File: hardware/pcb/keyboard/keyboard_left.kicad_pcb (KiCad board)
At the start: 2 copper layers, 133.8 x 110.4 mm, 109 parts, among them J1 SM04B-SRSS-TB, J2 PJ320D, J3 HRO_TYPE-C-31-M-12, J4 FH34SRJ-10S-0.5SH, SW29 PTS845, U1 74HC4051, U2 OPA350UA, U3 DT1446-04S, U4 XC6220B331MR-G, U5 STM32G0B1KETx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

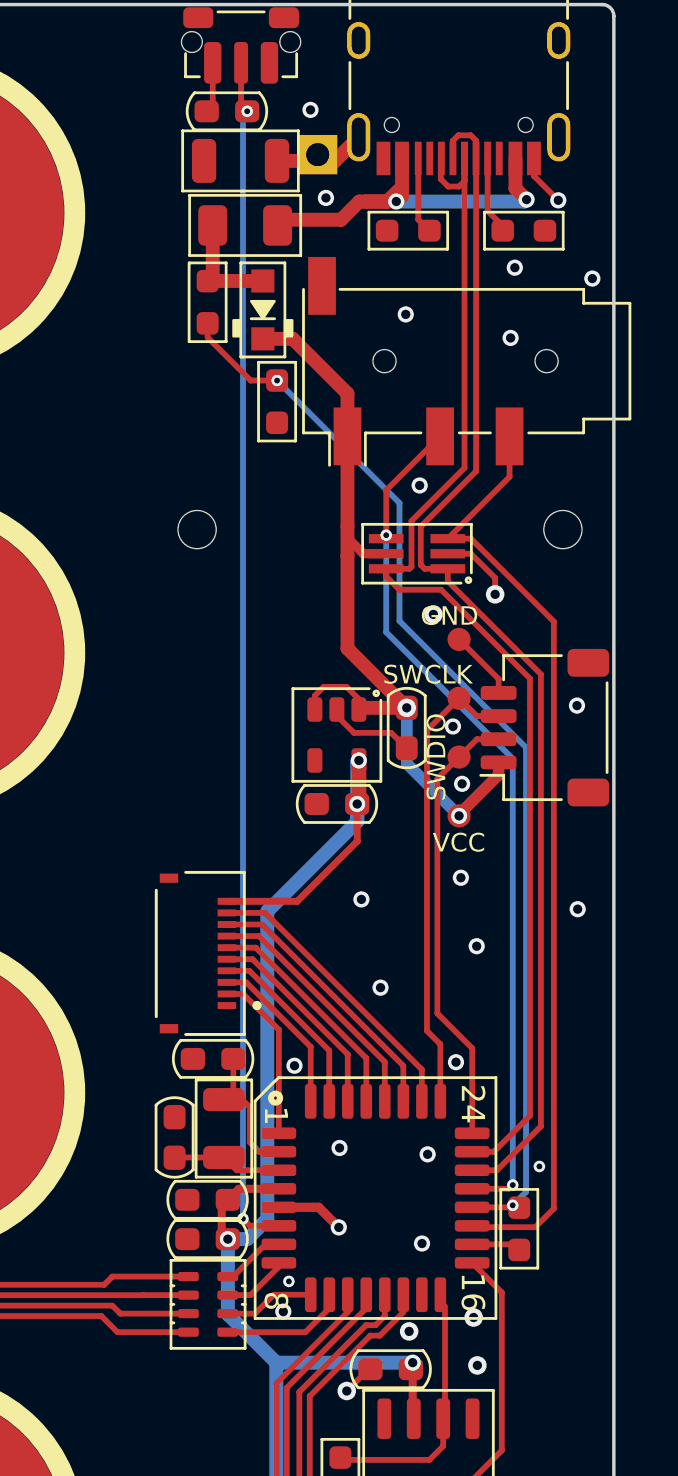
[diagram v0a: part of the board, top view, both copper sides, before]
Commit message: roate FFC Connector
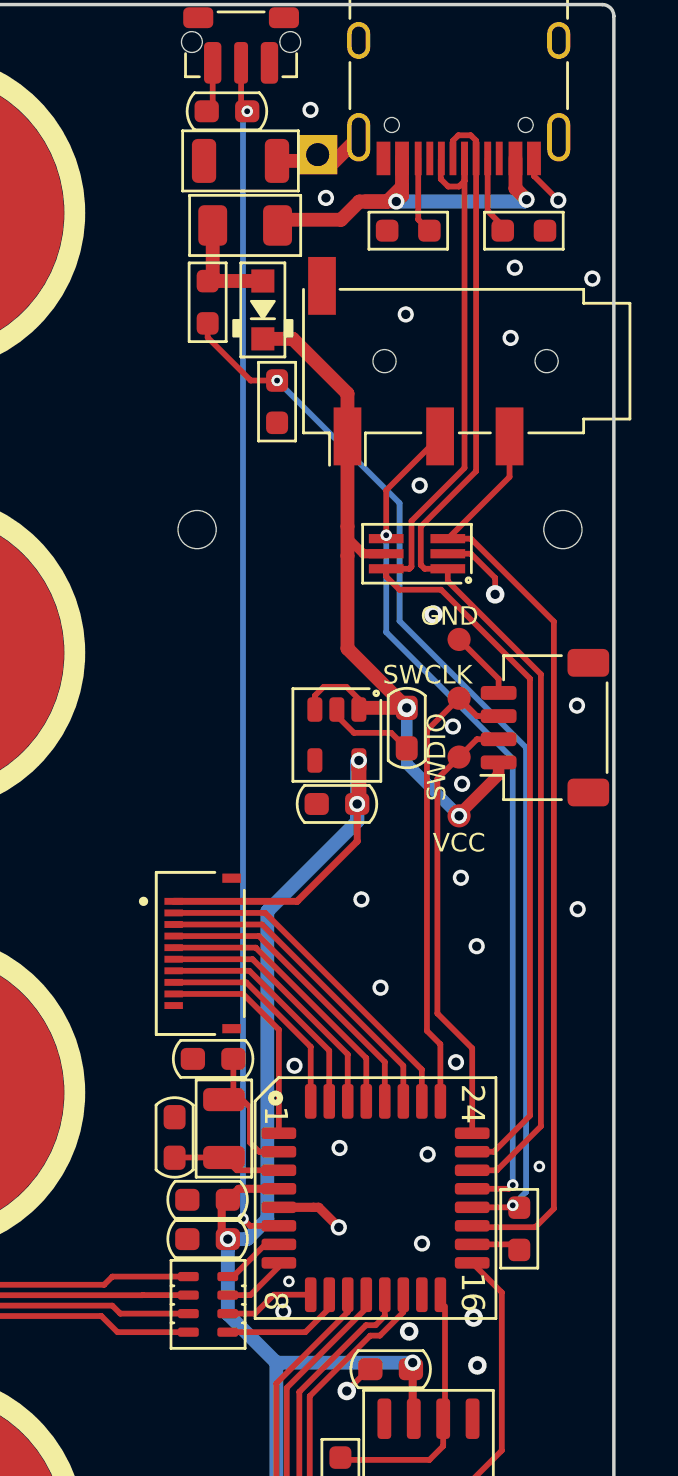
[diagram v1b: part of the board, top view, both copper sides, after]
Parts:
- turned J4 to 90 degrees
- turned RN3 to 180 degrees
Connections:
- net Handness renamed Handedness
- J4 pad 1: GND -> +3V3
- J4 pad 10: +3V3 -> GND
- J4 pad 2: ACCS_8 -> ACCS_1
- J4 pad 3: ACCS_7 -> ACCS_2
- J4 pad 4: ACCS_6 -> ACCS_3
- J4 pad 5: ACCS_5 -> ACCS_4
- J4 pad 6: ACCS_4 -> ACCS_5
- J4 pad 7: ACCS_3 -> ACCS_6
- J4 pad 8: ACCS_2 -> ACCS_7
- J4 pad 9: ACCS_1 -> ACCS_8
- RN3 pad 1: TX0 -> TX3
- RN3 pad 2: TX1 -> TX2
- RN3 pad 3: TX2 -> TX1
- RN3 pad 4: TX3 -> TX0
- RN3 pad 5: ROW3 -> ROW0
- RN3 pad 6: ROW2 -> ROW1
- RN3 pad 7: ROW1 -> ROW2
- RN3 pad 8: ROW0 -> ROW3
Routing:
- net +3V3: track 74.1 -> 76.5 mm
- net ACCS_8: track 7.35 -> 9.65 mm
- net ACCS_6: track 8.04 -> 10.3 mm
- net ACCS_5: track 8.95 -> 11.3 mm
- net ACCS_4: track 9.86 -> 12.2 mm
- net ACCS_3: track 10.8 -> 13.1 mm
- net ACCS_2: track 11.7 -> 14.0 mm
- net ACCS_1: track 12.6 -> 14.9 mm
- net ACCS_7: track 7.13 -> 9.43 mm

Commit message: temp
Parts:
- removed R1, R5: 1k, PCM_Resistor_SMD_AKL:R_0603_1608Metric_Pad0.98x0.95mm
- removed R4: < 800, PCM_Resistor_SMD_AKL:R_0603_1608Metric_Pad0.98x0.95mm
- added C11: 1uF, PCM_Capacitor_SMD_AKL:C_0603_1608Metric, F.Cu at (187.9, 55.0)
- added C12: 22p, PCM_Capacitor_SMD_AKL:C_0603_1608Metric, F.Cu at (183.5, 52.5)
- added C13: 22p, PCM_Capacitor_SMD_AKL:C_0603_1608Metric, F.Cu at (182.8, 58.2)
- added C14: 1uF, PCM_Capacitor_SMD_AKL:C_0603_1608Metric, F.Cu at (186.4, 55.0)
- added C16: 100n, PCM_Capacitor_SMD_AKL:C_0603_1608Metric, F.Cu at (193.3, 84.8)
- added C17: 1u, PCM_Capacitor_SMD_AKL:C_0603_1608Metric, F.Cu at (193.3, 86.6)
- added FB1: 1k 100mhz, Inductor_SMD:L_0603_1608Metric, F.Cu at (195.6, 85.6)
- added R8: 10k, PCM_Resistor_SMD_AKL:R_0603_1608Metric, F.Cu at (182.1, 80.0)
- added U6: CH334R, Package_SO:QSOP-16_3.9x4.9mm_P0.635mm, F.Cu at (187.4, 60.3)
- added Y2: 8MHz, PCM_Crystal_Handsoldering_AKL:Crystal_SMD_2520-4Pin_2.5x2.0mm, F.Cu at (183.7, 55.0)
- C1, C10, C2, C3, C4, C6, C7, C8, C9: footprint PCM_Capacitor_SMD_AKL:C_0603_1608Metric_Pad1.05x0.95mm -> PCM_Capacitor_SMD_AKL:C_0603_1608Metric
- C5: value 4.7u -> 0.1uF; footprint PCM_Capacitor_SMD_AKL:C_0603_1608Metric_Pad1.05x0.95mm -> PCM_Capacitor_SMD_AKL:C_0603_1608Metric
- R2, R3, R6, R7: footprint PCM_Resistor_SMD_AKL:R_0603_1608Metric_Pad0.98x0.95mm -> PCM_Resistor_SMD_AKL:R_0603_1608Metric
- U5: value STM32G0B1KETx -> STM32G431KBTx; footprint PCM_Package_QFP_AKL:LQFP-32_7x7mm_P0.8mm -> Package_QFP:LQFP-32_7x7mm_P0.8mm
- Y1: value NX3215SA -> 8MHz; footprint PCM_Crystal_AKL:Crystal_SMD_3215-2Pin_3.2x1.5mm -> PCM_Crystal_Handsoldering_AKL:Crystal_SMD_2520-4Pin_2.5x2.0mm
- moved H14 15.8 mm to (182.0, 48.9)
- moved H15 15.8 mm to (197.8, 48.9)
- moved C4 12.8 mm to (195.1, 83.1), turned to 0 degrees
- moved C8 9.40 mm to (186.9, 52.5), turned to 0 degrees
- moved U4 9.29 mm to (186.6, 49.7), turned to 180 degrees
- moved C9 6.87 mm to (189.5, 51.9)
- moved C5 5.88 mm to (185.1, 73.7), turned to 90 degrees
- moved D1 4.60 mm to (185.0, 45.1)
- moved F1 3.69 mm to (185.0, 40.4), turned to 90 degrees
- moved C7 2.46 mm to (182.4, 78.3), turned to 180 degrees
- moved U3 1.83 mm to (192.8, 49.7)
- moved L1 1.71 mm to (185.0, 35.4), turned to 90 degrees
- moved C1 1.47 mm to (184.8, 31.9), turned to 180 degrees
- moved R6 1.44 mm to (186.8, 94.2)
- moved C2 1.38 mm to (189.0, 86.3)
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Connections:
- C6 pad 2: /OSC32_IN -> Net-(U5-PF0)
- C7 pad 2: /OSC32_OUT -> Net-(U5-PF1)
- D1 pad 2: Net-(D1-A) -> VBUS
- F1 pad 1: Net-(D1-A) -> VBUS
- F1 pad 2: VBUS -> Net-(F1-Pad2)
- J1 pad 1: +5V -> +3V3
- J3 pad A4: VBUS -> Net-(F1-Pad2)
- J3 pad A6: D+ -> /UP_D+
- J3 pad A7: D- -> /UP_D-
- J3 pad A9: VBUS -> Net-(F1-Pad2)
- J3 pad B4: VBUS -> Net-(F1-Pad2)
- J3 pad B6: D+ -> /UP_D+
- J3 pad B7: D- -> /UP_D-
- J3 pad B9: VBUS -> Net-(F1-Pad2)
- J4 pad 2: ACCS_1 -> unconnected-(J4-Pin_2-Pad2)
- J4 pad 3: ACCS_2 -> ACCS_1
- J4 pad 4: ACCS_3 -> ACCS_2
- J4 pad 5: ACCS_4 -> ACCS_3
- J4 pad 6: ACCS_5 -> ACCS_4
- J4 pad 7: ACCS_6 -> ACCS_5
- J4 pad 8: ACCS_7 -> ACCS_6
- J4 pad 9: ACCS_8 -> ACCS_7
- TP1 pad 1: +5V -> +3V3
- U3 pad 1: D- -> USART_RX
- U3 pad 4: USART_RX -> /UP_D-
- U3 pad 6: D+ -> /UP_D+
- U5 pad 1: ACCS_8 -> +3V3
- U5 pad 10: TX3 -> CSEL1
- U5 pad 11: CSEL0 -> CSEL2
- U5 pad 12: CSEL1 -> CSEL_EN
- U5 pad 13: CSEL2 -> ADC
- U5 pad 14: CSEL_EN -> GND
- U5 pad 15: /ADC1_IN8 -> VDDA
- U5 pad 16: ADC -> GND
- U5 pad 17: CHARGE_RST -> +3V3
- U5 pad 18: Handedness -> CHARGE_RST
- U5 pad 2: /OSC32_IN -> Net-(U5-PF0)
- U5 pad 20: VBUS_DEC -> USART_RX
- U5 pad 21: USART_RX -> /MCU_D-
- U5 pad 22: D- -> /MCU_D+
- U5 pad 23: D+ -> SWDIO
- U5 pad 24: SWDIO -> SWCLK
- U5 pad 25: SWCLK -> ACCS_1
- U5 pad 26: ACCS_1 -> ACCS_2
- U5 pad 27: ACCS_2 -> ACCS_3
- U5 pad 28: ACCS_3 -> ACCS_4
- U5 pad 29: ACCS_4 -> ACCS_5
- U5 pad 3: /OSC32_OUT -> Net-(U5-PF1)
- U5 pad 30: ACCS_5 -> ACCS_6
- U5 pad 31: ACCS_6 -> ACCS_7
- U5 pad 32: ACCS_7 -> GND
- U5 pad 4: +3V3 -> /NRST
- U5 pad 5: GND -> TX0
- U5 pad 6: /NRST -> TX1
- U5 pad 7: TX0 -> TX2
- U5 pad 8: TX1 -> TX3
- U5 pad 9: TX2 -> CSEL0
- Y1 pad 1: /OSC32_IN -> Net-(U5-PF1)
- Y1 pad 2: /OSC32_OUT -> GND
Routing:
- net D+: track 53.2 -> 0.00 mm
- net D-: track 52.0 -> 0.00 mm
- net VBUS_DEC: track 46.5 -> 0.00 mm, vias 2 -> 0
- net +3V3: track 76.5 -> 113.8 mm, vias 5 -> 8
- net /UP_D+: track 0.00 -> 31.3 mm
- net /UP_D-: track 0.00 -> 30.2 mm
- net /MCU_D-: track 0.00 -> 22.9 mm
- net Net-(F1-Pad2): track 0.00 -> 19.5 mm, vias 0 -> 2
- net /MCU_D+: track 0.00 -> 18.6 mm
- net +5V: track 35.9 -> 18.8 mm
- net GND: track 20.6 -> 8.58 mm, vias 38 -> 25
- net ACCS_8: track 9.65 -> 0.00 mm
- net VDDA: track 0.00 -> 7.40 mm
- net Net-(U5-PF1): track 0.00 -> 6.50 mm
- net /OSC32_IN: track 6.12 -> 0.00 mm
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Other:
- board text added: "SWC"
- board text added: "SWD"
- board text removed: "SWCLK"
- board text removed: "SWDIO"

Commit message: Left init
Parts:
- added C15: 4.7 uF, PCM_Capacitor_SMD_AKL:C_0603_1608Metric, F.Cu at (187.6, 72.8)
- C16: value 100n -> 10n
- FB1: value 1k 100mhz -> 1kΩ 100mhz
- J4: footprint ec_parts:HRS_FH34SRJ-10S-0.5SH(50) -> ec_parts:HRS_FH34SRJ-12S-0.5SH(50)
- moved J4 0.50 mm to (182.1, 67.8)
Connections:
- J4 pad 1: +3V3 -> VBUS
- J4 pad 10: GND -> ACCS_6
- J4 pad 2: unconnected-(J4-Pin_2-Pad2) -> /DM4
- J4 pad 3: ACCS_1 -> /DP4
- J4 pad 4: ACCS_2 -> +3V3
- J4 pad 5: ACCS_3 -> ACCS_1
- J4 pad 6: ACCS_4 -> ACCS_2
- J4 pad 7: ACCS_5 -> ACCS_3
- J4 pad 8: ACCS_6 -> ACCS_4
- J4 pad 9: ACCS_7 -> ACCS_5
- U6 pad 1: unconnected-(U6-DM4-Pad1) -> /DM4
- U6 pad 2: unconnected-(U6-DP4-Pad2) -> /DP4
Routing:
- net VBUS: track 17.1 -> 28.4 mm
- net /DP4: track 0.00 -> 7.26 mm
- net +3V3: track 113.8 -> 120.3 mm, vias 8 -> 9
- net /DM4: track 0.00 -> 6.36 mm
- net /UP_D+: track 31.3 -> 27.5 mm
- net GND: track 8.58 -> 10.6 mm, vias 25 -> 35
- net ACCS_7: track 9.23 -> 10.0 mm
- net TX0: track 4.48 -> 3.86 mm
- net CHARGE_RST: track 27.5 -> 26.9 mm
- net Net-(U5-PF1): track 6.50 -> 5.92 mm
- net ACCS_4: track 12.3 -> 12.9 mm
- net Net-(U6-XO): track 5.87 -> 5.36 mm
- net ACCS_6: track 10.3 -> 10.6 mm, vias 0 -> 2
- net ACCS_5: track 11.3 -> 11.5 mm, vias 0 -> 2

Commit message: Right init
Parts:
- moved C16 2.89 mm to (196.2, 84.9)
- moved C17 2.45 mm to (193.8, 84.2), turned to 90 degrees
- moved FB1 2.42 mm to (196.2, 83.3), turned to 0 degrees
- moved C4 2.14 mm to (196.4, 81.4)
- moved R8 1.39 mm to (183.1, 79.0), turned to -90 degrees
- moved C7 1.22 mm to (181.4, 79.0), turned to 90 degrees
- moved C2 0.68 mm to (188.3, 86.5)
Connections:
- C1 pad 1: GND -> A5
- C10 pad 2: GND -> A5
- C11 pad 2: GND -> A5
- C12 pad 1: GND -> A5
- C13 pad 1: GND -> A5
- C14 pad 2: GND -> A5
- C15 pad 2: GND -> A5
- C16 pad 2: GND -> A5
- C17 pad 2: GND -> A5
- C2 pad 1: GND -> A5
- C3 pad 1: GND -> A5
- C4 pad 2: GND -> A5
- C5 pad 2: GND -> A5
- C6 pad 1: GND -> A5
- C7 pad 1: GND -> A5
- C8 pad 2: GND -> A5
- C9 pad 2: GND -> A5
- H0 pad 1: GND -> A5
- J1 pad 4: GND -> A5
- J1 pad MP: GND -> A5
- J2 pad S: GND -> A5
- J3 pad A1: GND -> A5
- J3 pad A12: GND -> A5
- J3 pad B1: GND -> A5
- J3 pad B12: GND -> A5
- J4 pad 12: GND -> A5
- L1 pad 1: GND -> A5
- R2 pad 2: GND -> A5
- R3 pad 2: GND -> A5
- R6 pad 2: GND -> A5
- RN1 pad 5: GND -> A5
- RN1 pad 6: GND -> A5
- RN1 pad 7: GND -> A5
- RN1 pad 8: GND -> A5
- RN2 pad 5: GND -> A5
- RN2 pad 6: GND -> A5
- RN2 pad 7: GND -> A5
- RN2 pad 8: GND -> A5
- SW1 pad 3: GND -> A5
- SW10 pad 3: GND -> A5
- SW11 pad 3: GND -> A5
- SW12 pad 3: GND -> A5
- SW13 pad 3: GND -> A5
- SW14 pad 3: GND -> A5
- SW15 pad 3: GND -> A5
- SW16 pad 3: GND -> A5
- SW17 pad 3: GND -> A5
- SW18 pad 3: GND -> A5
- SW19 pad 3: GND -> A5
- SW2 pad 3: GND -> A5
- SW20 pad 3: GND -> A5
- SW21 pad 3: GND -> A5
- SW22 pad 3: GND -> A5
- SW23 pad 3: GND -> A5
- SW24 pad 3: GND -> A5
- SW25 pad 3: GND -> A5
- SW26 pad 3: GND -> A5
- SW27 pad 3: GND -> A5
- SW28 pad 3: GND -> A5
- SW29 pad 1: GND -> A5
- SW3 pad 3: GND -> A5
- SW4 pad 3: GND -> A5
- SW5 pad 3: GND -> A5
- SW6 pad 3: GND -> A5
- SW7 pad 3: GND -> A5
- SW8 pad 3: GND -> A5
- SW9 pad 3: GND -> A5
- TP1 pad 4: GND -> A5
- U1 pad 7: GND -> A5
- U1 pad 8: GND -> A5
- U2 pad 4: GND -> A5
- U3 pad 2: GND -> A5
- U4 pad 2: GND -> A5
- U5 pad 12: CSEL_EN -> ADC
- U5 pad 13: ADC -> CHARGE_RST
- U5 pad 14: GND -> A5
- U5 pad 16: GND -> A5
- U5 pad 18: CHARGE_RST -> CSEL_EN
- U5 pad 32: GND -> A5
- U6 pad 14: GND -> A5
- Y1 pad 2: GND -> A5
- Y1 pad 4: GND -> A5
- Y2 pad 2: GND -> A5
- Y2 pad 4: GND -> A5
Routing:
- net A5: track 0.00 -> 37.8 mm, vias 0 -> 37
- net GND: track 10.6 -> 0.00 mm, vias 35 -> 0
- net /NRST: track 56.0 -> 50.9 mm
- net CHARGE_RST: track 26.9 -> 22.7 mm
- net /UP_D+: track 27.5 -> 30.4 mm
- net +3V3: track 120.3 -> 118.7 mm
- net VDDA: track 7.40 -> 6.41 mm
- net CSEL_EN: track 22.5 -> 21.9 mm, vias 0 -> 2
- added copper zone on B.Cu, net A5
- added copper zone on F.Cu, net A5
- removed copper zone on B.Cu, net GND
- removed copper zone on F.Cu, net GND

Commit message: usb hib init
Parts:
- added R1: 10k, PCM_Resistor_SMD_AKL:R_0603_1608Metric, F.Cu at (182.2, 62.2)
- added R4: 5.1k, PCM_Resistor_SMD_AKL:R_0603_1608Metric, F.Cu at (182.2, 60.5)
- J4: value FH34SRJ-10S-0.5SH -> FH34SRJ-12S-0.5SH
- moved C13 0.73 mm to (182.9, 57.5), turned to 180 degrees
- moved H14 0.41 mm to (182.0, 48.5)
- moved H15 0.41 mm to (197.8, 48.5)
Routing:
- net ACCS_3: track 13.8 -> 22.7 mm
- net VBUS: track 28.4 -> 27.8 mm
- net A5: track 37.8 -> 37.5 mm, vias 37 -> 36
- net +3V3: track 118.7 -> 118.5 mm, vias 9 -> 10

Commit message: preproduction
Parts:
- C12, C13, C6, C7: value 22p -> 10pF
- U3: value DT1446-04S -> PRTR5V0U2X; footprint PCM_Package_TO_SOT_SMD_AKL:SOT-363_SC-70-6_Handsoldering -> PCM_Package_TO_SOT_SMD_AKL:SOT-143
- Y2: value 8MHz -> 12MHz
- moved R2 0.56 mm to (196.7, 37.0)
- moved R3 0.55 mm to (190.2, 37.0)
- moved U3 0.26 mm to (192.5, 49.7)
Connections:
- U3 pad 1: USART_RX -> A5
- U3 pad 2: A5 -> /UP_D-
- U3 pad 3: USART_TX -> /UP_D+
- U3 pad 4: /UP_D- -> +5V
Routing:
- net +5V: track 18.4 -> 14.3 mm
- net /UP_D-: track 30.0 -> 31.8 mm
- net USART_TX: track 38.8 -> 37.2 mm
- net A5: track 37.5 -> 36.2 mm, vias 36 -> 37
- net /UP_D+: track 30.4 -> 29.5 mm
- net Net-(J3-CC2): track 2.64 -> 3.29 mm
- net USART_RX: track 38.1 -> 37.6 mm

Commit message: temp
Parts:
- RN1, RN2: value 1k R_Array_Concave_4x0603 -> 100k R_Array_Concave_4x0603
- U6: footprint Package_SO:QSOP-16_3.9x4.9mm_P0.635mm -> PCM_Package_SO_AKL:QSOP-16_3.9x4.9mm_P0.635mm
- Y1: value 8MHz -> 8MHz 10pF

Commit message: rev2
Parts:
- removed C11, C14: 1uF, PCM_Capacitor_SMD_AKL:C_0603_1608Metric
- removed C12, C13: 10pF, PCM_Capacitor_SMD_AKL:C_0603_1608Metric
- removed U6: CH334R, PCM_Package_SO_AKL:QSOP-16_3.9x4.9mm_P0.635mm
- removed Y2: 12MHz, PCM_Crystal_Handsoldering_AKL:Crystal_SMD_2520-4Pin_2.5x2.0mm
- J1: value SM04B-SRSS-TB -> SM03B-SRSS-TB; footprint Connector_JST:JST_SH_SM04B-SRSS-TB_1x04-1MP_P1.00mm_Horizontal -> Connector_JST:JST_SH_SM03B-SRSS-TB_1x03-1MP_P1.00mm_Horizontal
- moved J1 0.50 mm to (197.0, 58.1)
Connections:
- J1 pad 1: +3V3 -> SWCLK
- J1 pad 2: SWDIO -> A5
- J1 pad 3: SWCLK -> SWDIO
- J1 pad MP: A5 -> unconnected-(J1-MountPin-PadMP)
- J3 pad A6: /UP_D+ -> D+
- J3 pad A7: /UP_D- -> D-
- J3 pad B6: /UP_D+ -> D+
- J3 pad B7: /UP_D- -> D-
- J4 pad 1: VBUS -> unconnected-(J4-Pin_1-Pad1)
- J4 pad 2: /DM4 -> +5V
- J4 pad 3: /DP4 -> +5V
- J4 pad 4: +3V3 -> unconnected-(J4-Pin_4-Pad4)
- J4 pad 9: ACCS_5 -> A5
- R1 pad 1: ACCS_3 -> PB6
- R4 pad 2: ACCS_3 -> PB6
- TP1 pad 2: SWDIO -> SWCLK
- TP1 pad 3: SWCLK -> A5
- TP1 pad 4: A5 -> SWDIO
- U3 pad 2: /UP_D- -> D-
- U3 pad 3: /UP_D+ -> D+
- U5 pad 21: /MCU_D- -> D-
- U5 pad 22: /MCU_D+ -> D+
- U5 pad 29: ACCS_5 -> PB6
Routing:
- net D-: track 0.00 -> 54.8 mm
- net D+: track 0.00 -> 52.2 mm
- net /UP_D-: track 31.8 -> 0.00 mm
- net /UP_D+: track 29.5 -> 0.00 mm
- net +5V: track 14.3 -> 37.9 mm, vias 2 -> 4
- net /MCU_D-: track 23.0 -> 0.00 mm
- net PB6: track 0.00 -> 18.8 mm, vias 0 -> 2
- net /MCU_D+: track 18.6 -> 0.00 mm
- net A5: track 36.2 -> 23.8 mm, vias 37 -> 40
- net ACCS_5: track 11.3 -> 0.00 mm, vias 2 -> 0
- net SWDIO: track 21.5 -> 30.9 mm
- net ACCS_3: track 22.7 -> 13.9 mm
- net /DP4: track 7.26 -> 0.00 mm
- net /DM4: track 6.36 -> 0.00 mm
- net VBUS: track 27.8 -> 21.5 mm
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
